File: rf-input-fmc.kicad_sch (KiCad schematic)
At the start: 2 parts, among them J1 SMA, J2 SMA

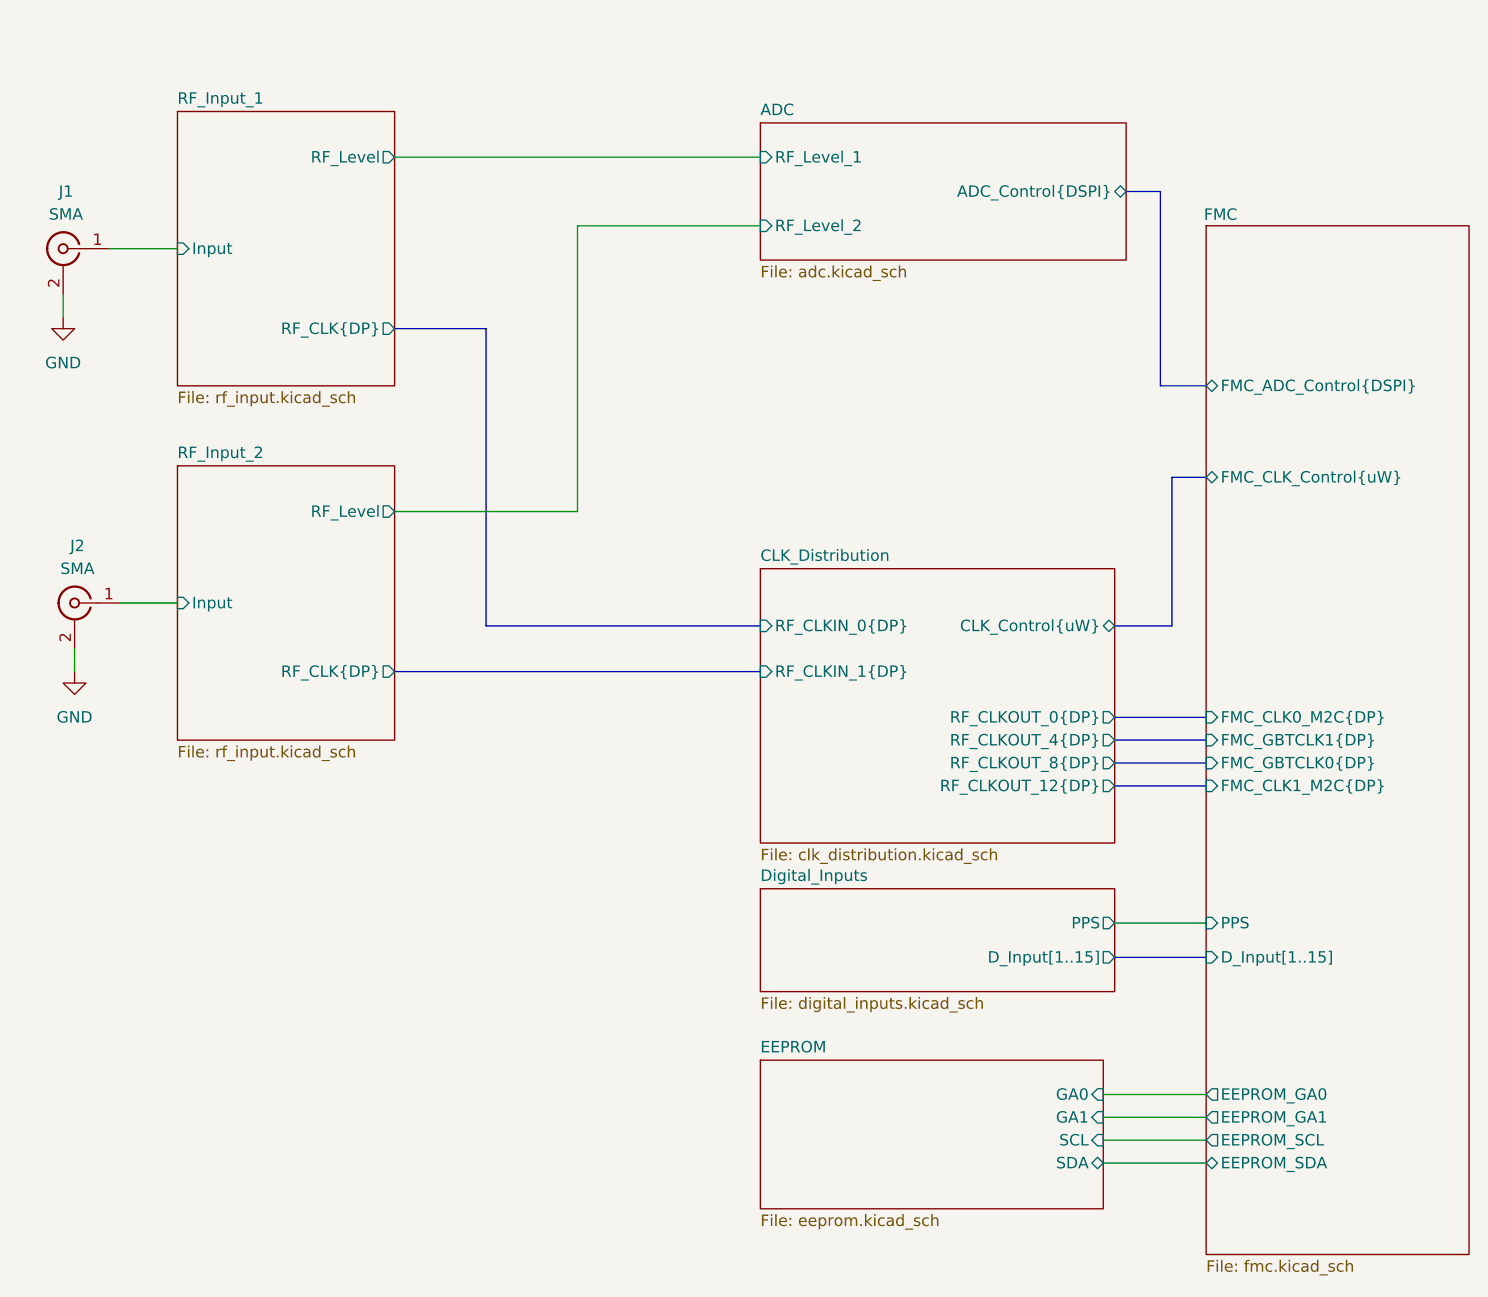
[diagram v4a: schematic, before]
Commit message: Changes to Based on Pre-Production Run
- Added FPGA control for digital input buffer's OE pin with pull up
- Grounded ref caps on ADC properly
- Swapped pins 5&6 on U7 (polarity fix)
- Fixed naming of CLK inputs to be  "CLK1" / "CLK2" to be clk0 & clk1 inputs on LMK
    - Changed "J" tag to be digital IO only "J1 - J16"
- Mounting Holes changed 3.0mm to match with Marble
- Added 50ohm non-populated resistors in on digital inputs

- Changed labeling of ADC inputs in schematic (no copper changes)
- Changed labeling/assignment of digital inputs on the FMC connector (almost no copper changes)
	- now J1 = Dinput1 ... J15= Dinput16; J16 = PPS (PPS has unchanged mapping)
- Swapped h37 and g37 pin assignments (new D15 &D14)
	- for better compatibility with new FMC template

These changes were covered by moving to the new FMC template:
- Add heartbeat LED
- Add SN on both sides
- Move SN and logo to template side of board
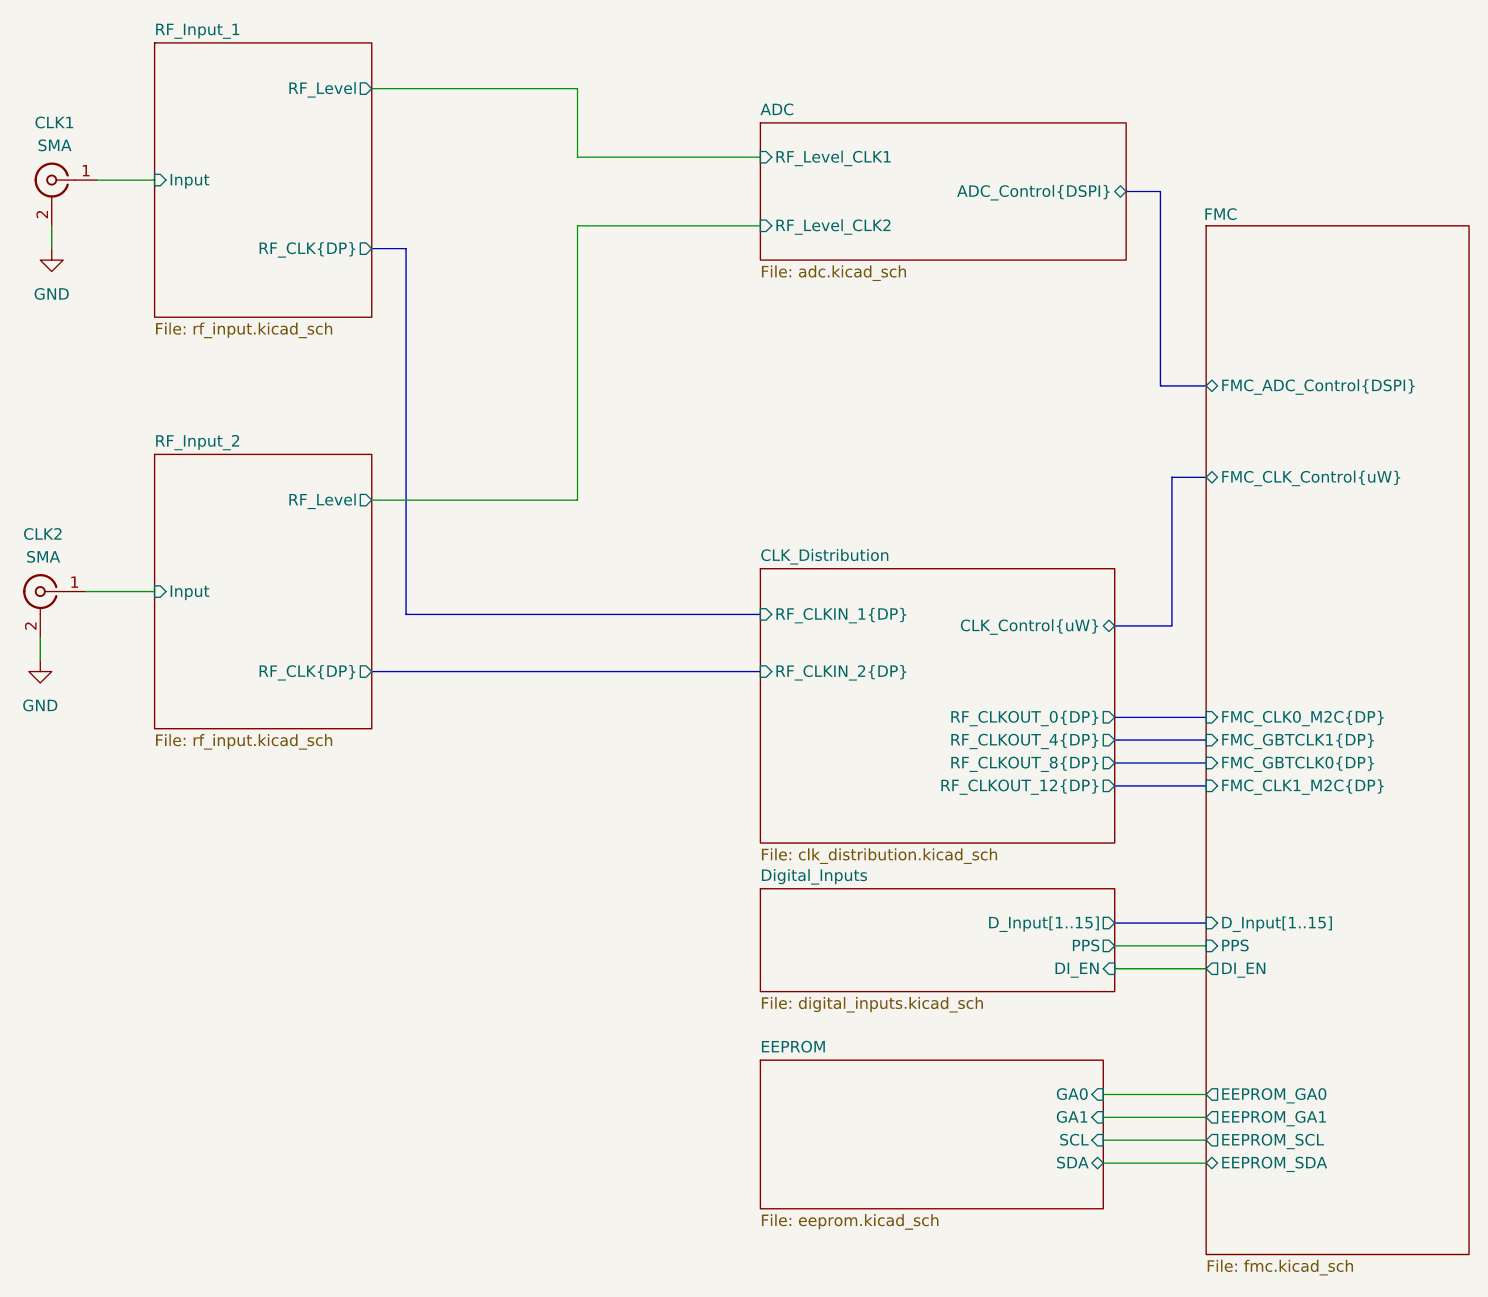
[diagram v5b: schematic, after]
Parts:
- renumbered J2 to CLK1, J1 to CLK2
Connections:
- net RF_Input_1/Input: now also CLK1.1 (In); no longer CLK2.1 (In)
- net RF_Input_2/Input: now also CLK2.1 (In); no longer CLK1.1 (In)
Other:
- sheet ADC ports: added RF_Level_CLK1, RF_Level_CLK2; removed RF_Level_1, RF_Level_2
- sheet CLK_Distribution ports: added RF_CLKIN_2{DP}; removed RF_CLKIN_0{DP}
- sheet Digital_Inputs ports: added DI_EN; removed none
- sheet FMC ports: added DI_EN; removed none
- moved on the sheet: CLK1, CLK2
